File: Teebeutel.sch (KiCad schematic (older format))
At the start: 37 parts, among them J1 RJ45_Shielded, J2 Conn_01x30_Female, J3 Micro_SD_Card, U1 ESP32-WROOM-32, U2 TLV1117-33, U3 MCP73831-2-OT, U4 SDB628, U5 LIS2DE12

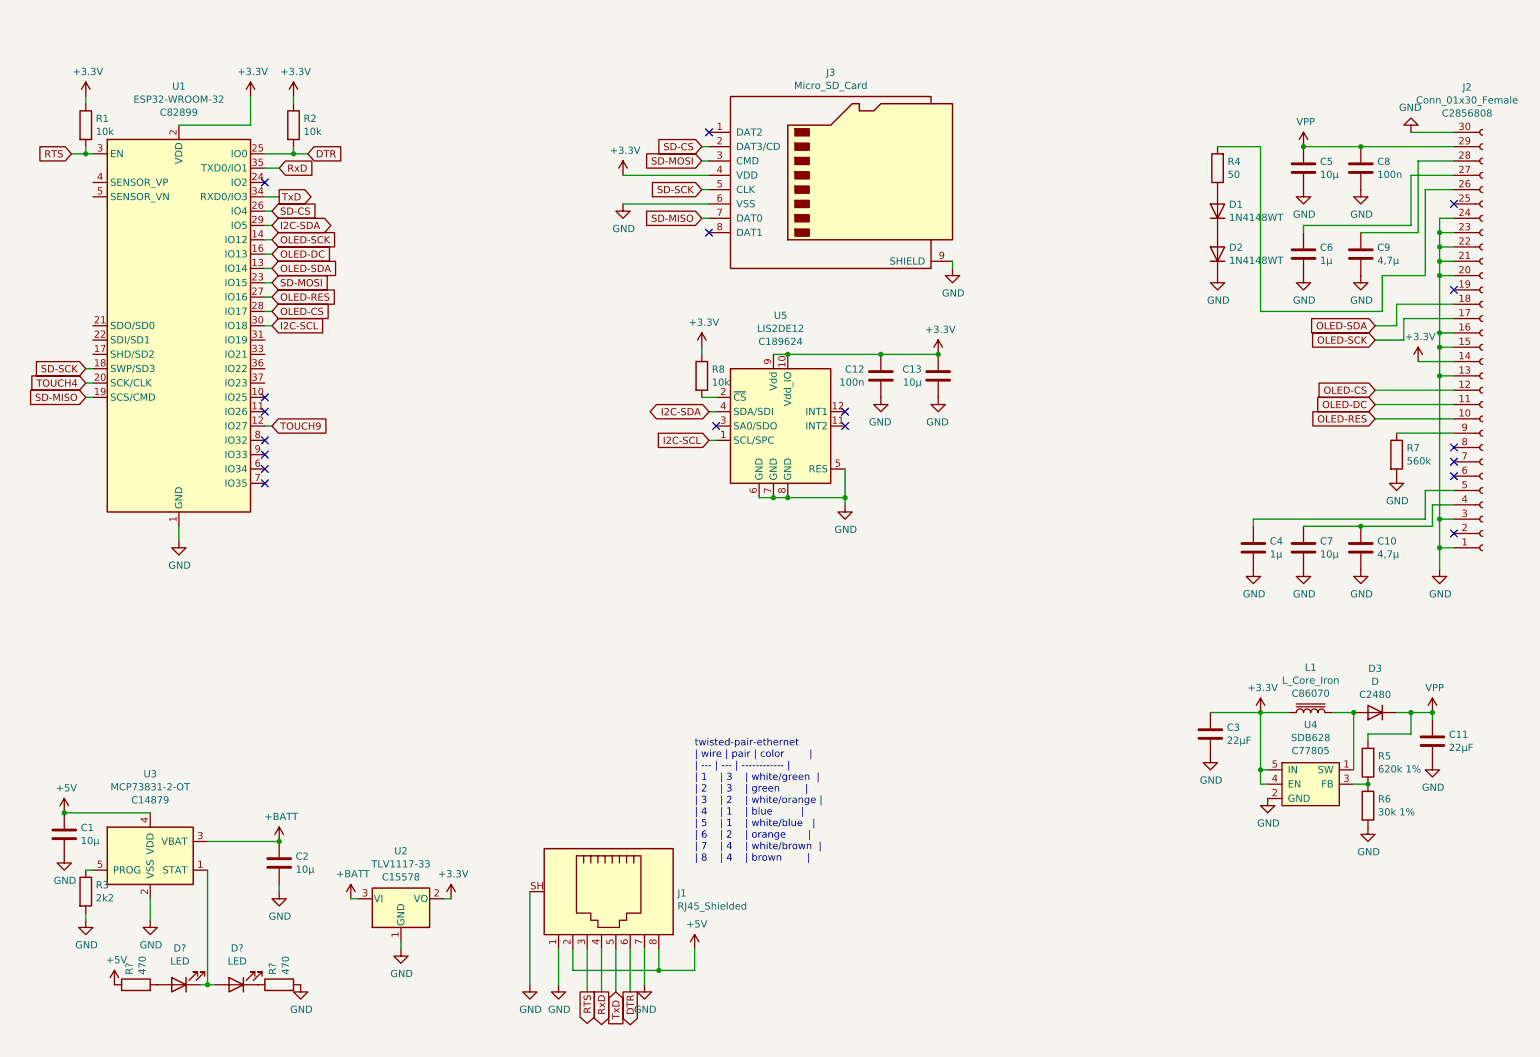
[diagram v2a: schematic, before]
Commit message: feat: add ws2812 leds
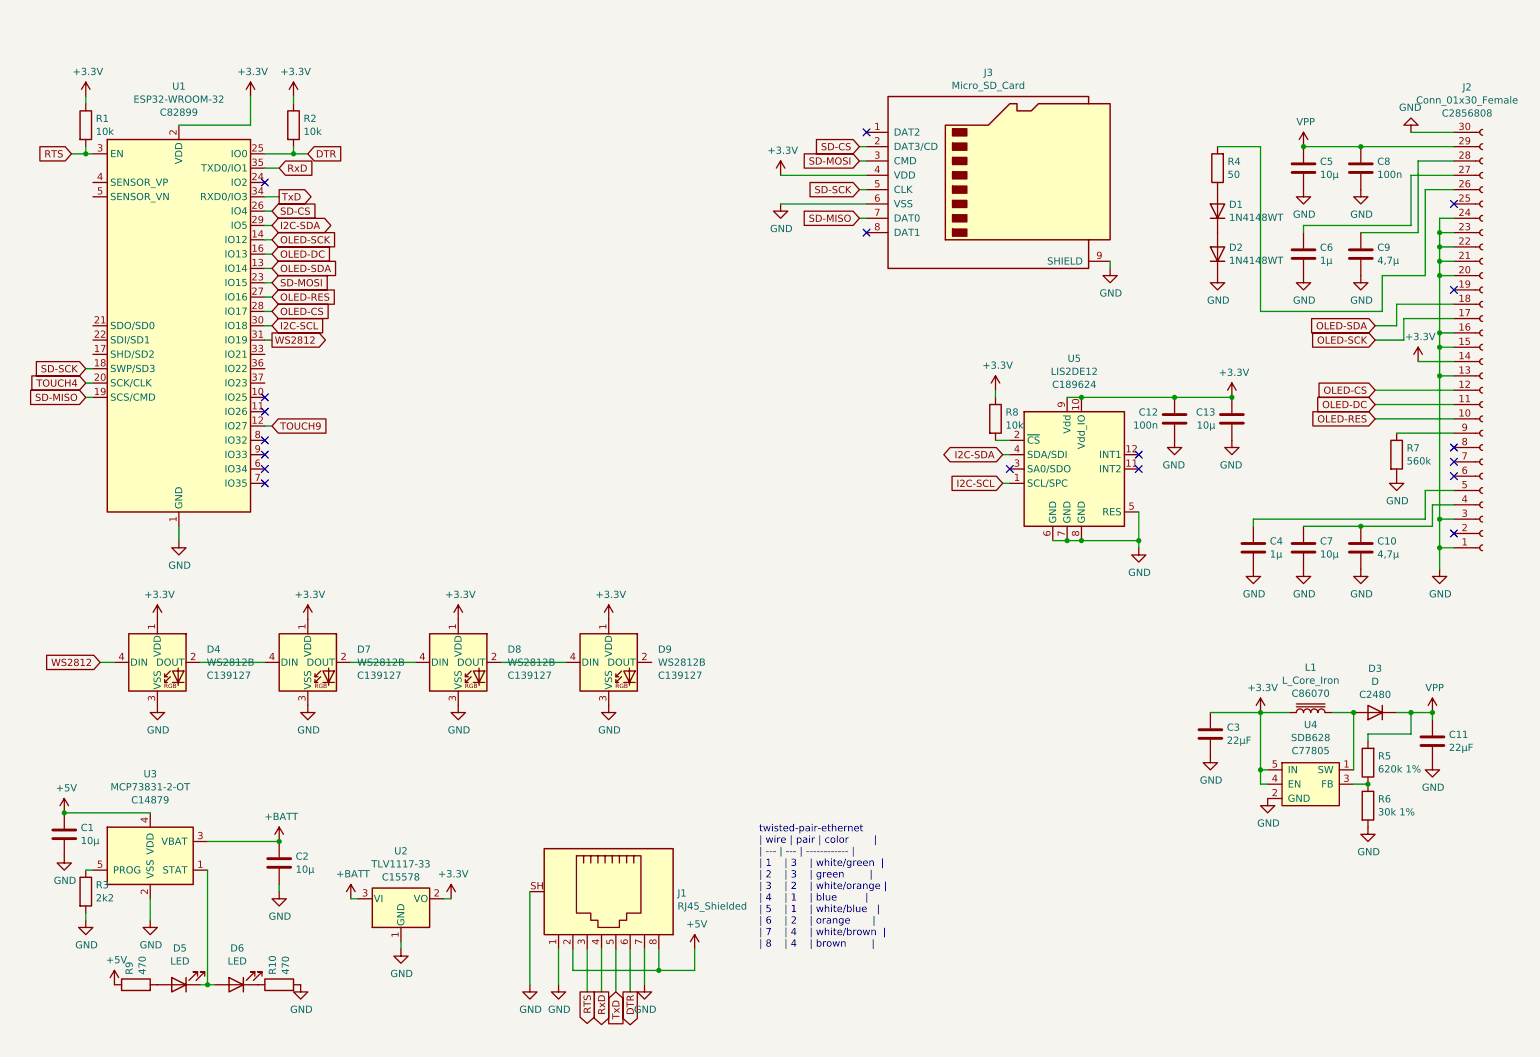
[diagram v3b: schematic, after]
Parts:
- added D4, D7, D8, D9: WS2812B, LED_SMD:LED_WS2812B_PLCC4_5.0x5.0mm_P3.2mm, symbol LED:WS2812B
- D5, D6: renamed from D?; footprint (none) -> LED_SMD:LED_1210_3225Metric
- gave numbers to parts that had none: 2
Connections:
- net +3V3: now also D4.1 (VDD), D7.1 (VDD), D8.1 (VDD), D9.1 (VDD)
- net GND: now also D4.3 (VSS), D7.3 (VSS), D8.3 (VSS), D9.3 (VSS)
- net WS2812: now reaches U1.31 (IO19)
- net WS2812: now also D4.4 (DIN)
- new net: D4.2 (DOUT), D7.4 (DIN)
- new net: D7.2 (DOUT), D8.4 (DIN)
- new net: D8.2 (DOUT), D9.4 (DIN)
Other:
- moved on the sheet: C12, C13, J3, R8, U5

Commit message: feat: add MORE sensors
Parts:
- added C14, C16, C18, C19: 100n, Capacitor_SMD:C_0603_1608Metric, symbol Device:C
- added C15, C17: 10µ, Capacitor_SMD:C_0603_1608Metric, symbol Device:C
- added R11, R12, R13, R14, R15, R16, R17, R18, R19, R20: 10k, Resistor_SMD:R_0603_1608Metric, symbol Device:R
- added SW1: K1-1506SN-01, custom_parts:K1-1506SN-01, symbol custom-parts:K1-1506SN-01
- added U6: TLV70018_SOT23-5, Package_TO_SOT_SMD:SOT-23-5, symbol Regulator_Linear:TLV70018_SOT23-5
- added U7: SGP30, custom_parts:SGP30, symbol custom-parts:SGP30
- added U8: PPSI262, custom_parts:PPSI262, symbol custom-parts:PPSI262
- added U9: TXB0104RUT, Package_DFN_QFN:Texas_R_PUQFN-N12, symbol Logic_LevelTranslator:TXB0104RUT
- J3: footprint Connector_Card:microSD_HC_Hirose_DM3AT-SF-PEJM5 -> (none); JLCPCB (none) -> C164170
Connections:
- net +3V3: now also C16.1, C17.1, C18.1, R11.1, R12.1, R13.1, R14.1, R15.1, R19.1, R20.1, U8.11 (TX_SUP), U8.16 (IO_SUP), U8.5 (RX_SUP), U9.1 (VCCA)
- net +BATT: now also U6.1 (IN), U6.3 (EN)
- net GND: now also C14.2, C15.2, C16.2, C17.2, C18.2, C19.2, R16.2, R17.2, R18.2, SW1.4 (COM), U6.2 (GND), U7.2 (GND), U8.15 (GND), U8.18 (CONTROL1), U9.6 (GND)
- net I2C-SCL: now also R20.2, U8.7 (CLK), U9.3 (A2)
- net I2C-SDA: now also R19.2, U8.8 (SDA), U9.2 (A1)
- net BTN_PUSH: now reaches U1.17 (SHD/SD2)
- net BTN_PUSH: now also R14.2, SW1.6 (CENTER)
- net BTN_UP: now reaches U1.21 (SDO/SD0)
- net BTN_UP: now also R13.2, SW1.1 (A_UP)
- net BTN_DOWN: now reaches U1.22 (SDI/SD1)
- net BTN_DOWN: now also R11.2, SW1.3 (C_DOWN)
- net BTN_LEFT: now reaches U1.33 (IO21)
- net BTN_LEFT: now also R12.2, SW1.2 (B_LEFT)
- net BTN_RIGHT: now reaches U1.36 (IO22)
- net BTN_RIGHT: now also R15.2, SW1.5 (D_RIGHT)
- new net: R17.1, U8.19 (I2C_SPI_SEL)
- new net: C19.1, U8.3 (BG)
- new net: R16.1, U8.6 (RESETZ)
- new net: U7.3 (SDA), U9.10 (B1)
- new net: U7.6 (SDC), U9.9 (B2)
- new net: R18.1, U9.12 (OE)
- new net +1V8: C14.1, C15.1, U6.5 (OUT), U7.1 (VDD), U7.5 (VDDH), U9.11 (VCCB)
- no-connect marks 18 -> 23
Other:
- note added: "twisted-pair-ethernet\n| wire | pair | color\n| --- | --- |\n| 1 | 3 | white/green\n| 2 | 3 | green\n| 3 | 2 | white/orange\n| 4 | 1 | blue\n| 5 | 1 | white/blue\n| 6 | 2 | orange\n| 7 | 4 | white/brown\n| 8 | 4 | brown"
- note removed: "twisted-pair-ethernet\n| wire | pair | color |\n| --- | --- | ------------ |\n| 1 | 3 | white/green |\n| 2 | 3 | green |\n| 3 | 2 | white/orange |\n| 4 | 1 | blue |\n| 5 | 1 | white/blue |\n| 6 | 2 | orange |\n| 7 | 4 | white/brown |\n| 8 | 4 | brown |"
- moved on the sheet: C12, C13, J1, R1, R2, R8, U1, U2, U5

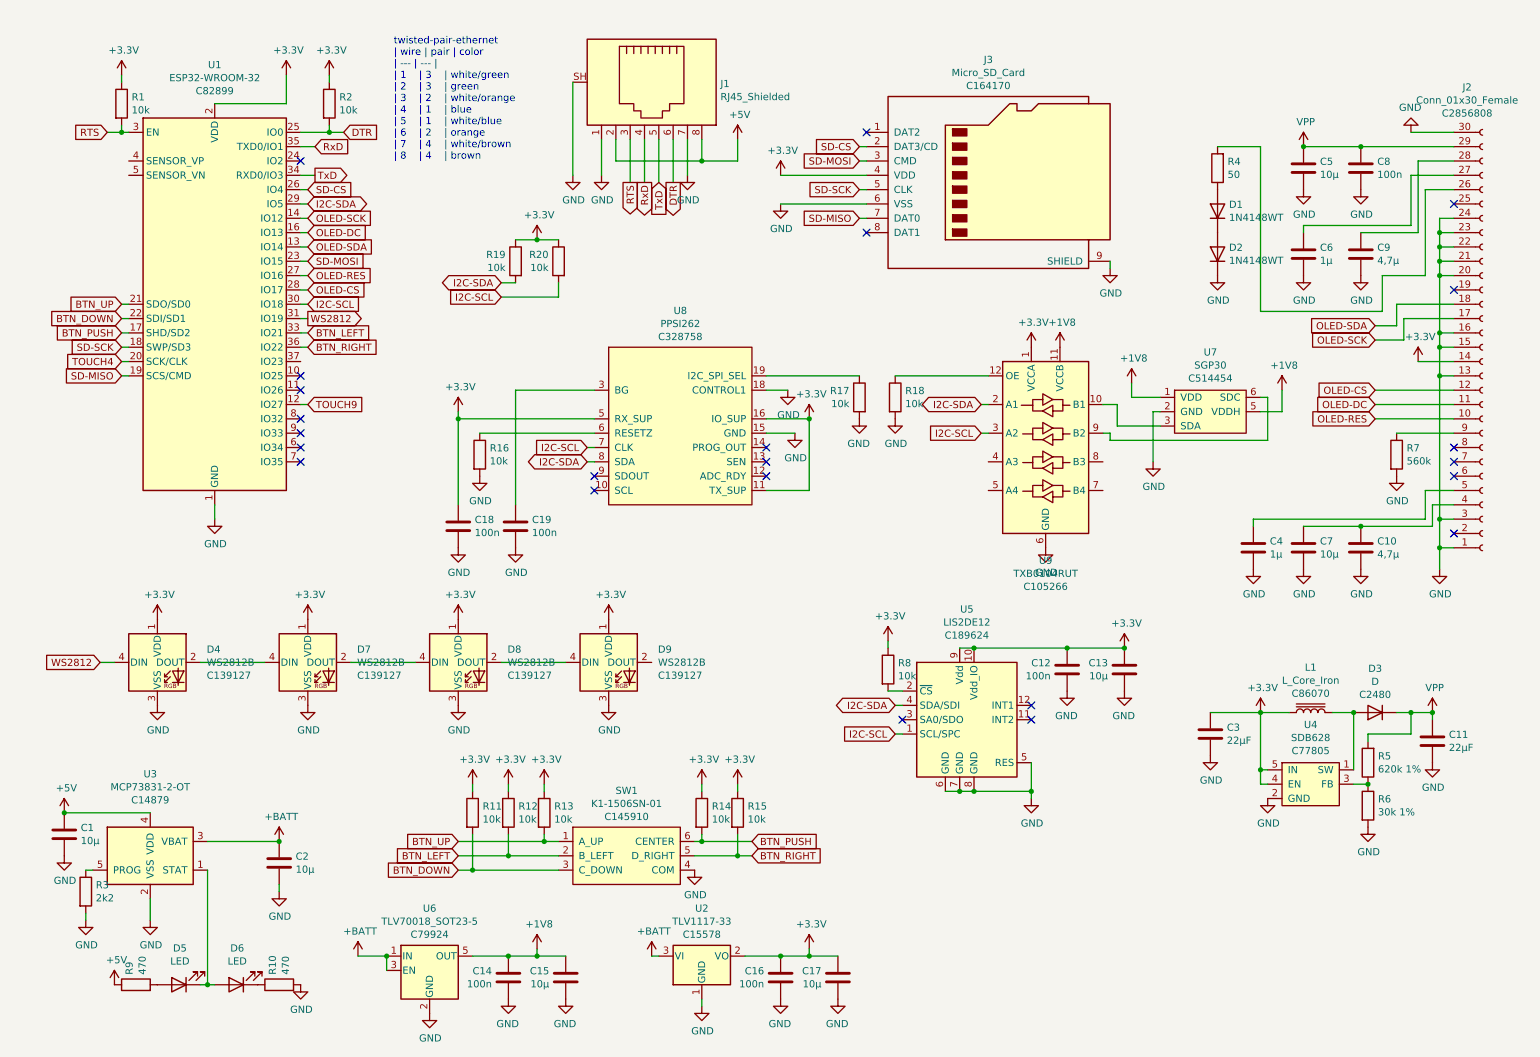
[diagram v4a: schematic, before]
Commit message: feat: add SD-Card footprint and some cleanup
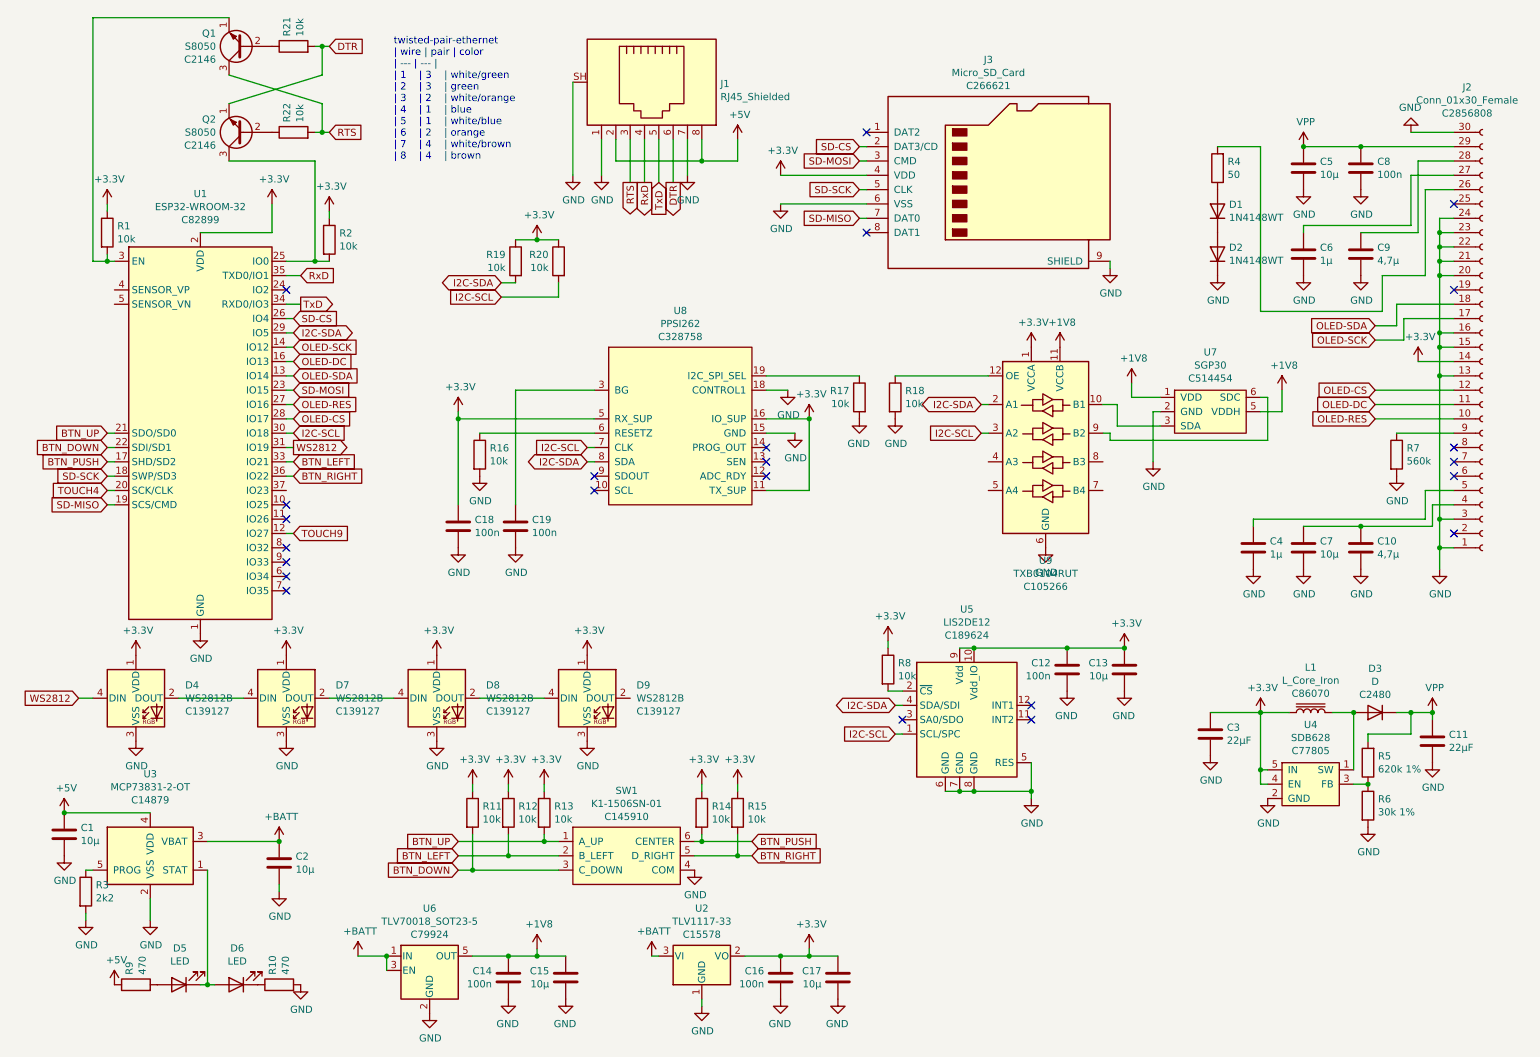
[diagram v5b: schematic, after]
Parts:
- added Q1, Q2: S8050, Package_TO_SOT_THT:TO-92_Inline, symbol Transistor_BJT:S8050
- added R21, R22: 10k, Resistor_SMD:R_0603_1608Metric, symbol Device:R
- J3: footprint (none) -> custom_parts:TF15X15; JLCPCB C164170 -> C266621
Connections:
- net DTR: now also Q2.1 (E), R21.2; no longer R2.2, U1.25 (IO0)
- net RTS: now also Q1.3 (C), R22.2; no longer R1.2, U1.3 (EN)
- new net: Q2.3 (C), R2.2, U1.25 (IO0)
- new net: Q1.1 (E), R1.2, U1.3 (EN)
- new net: Q2.2 (B), R22.1
- new net: Q1.2 (B), R21.1
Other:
- moved on the sheet: D4, D7, D8, D9, R1, R2, U1
